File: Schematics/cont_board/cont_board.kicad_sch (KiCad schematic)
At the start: 30 parts, among them IC1 LM2931AZ-5.0_TO92, J1 Conn_01x04, J2 Conn_01x04, J3 Conn_01x04, J4 Conn_01x04, SW1 SW_SPDT, U1 LM317_TO-220, U2 MCP23017_SP

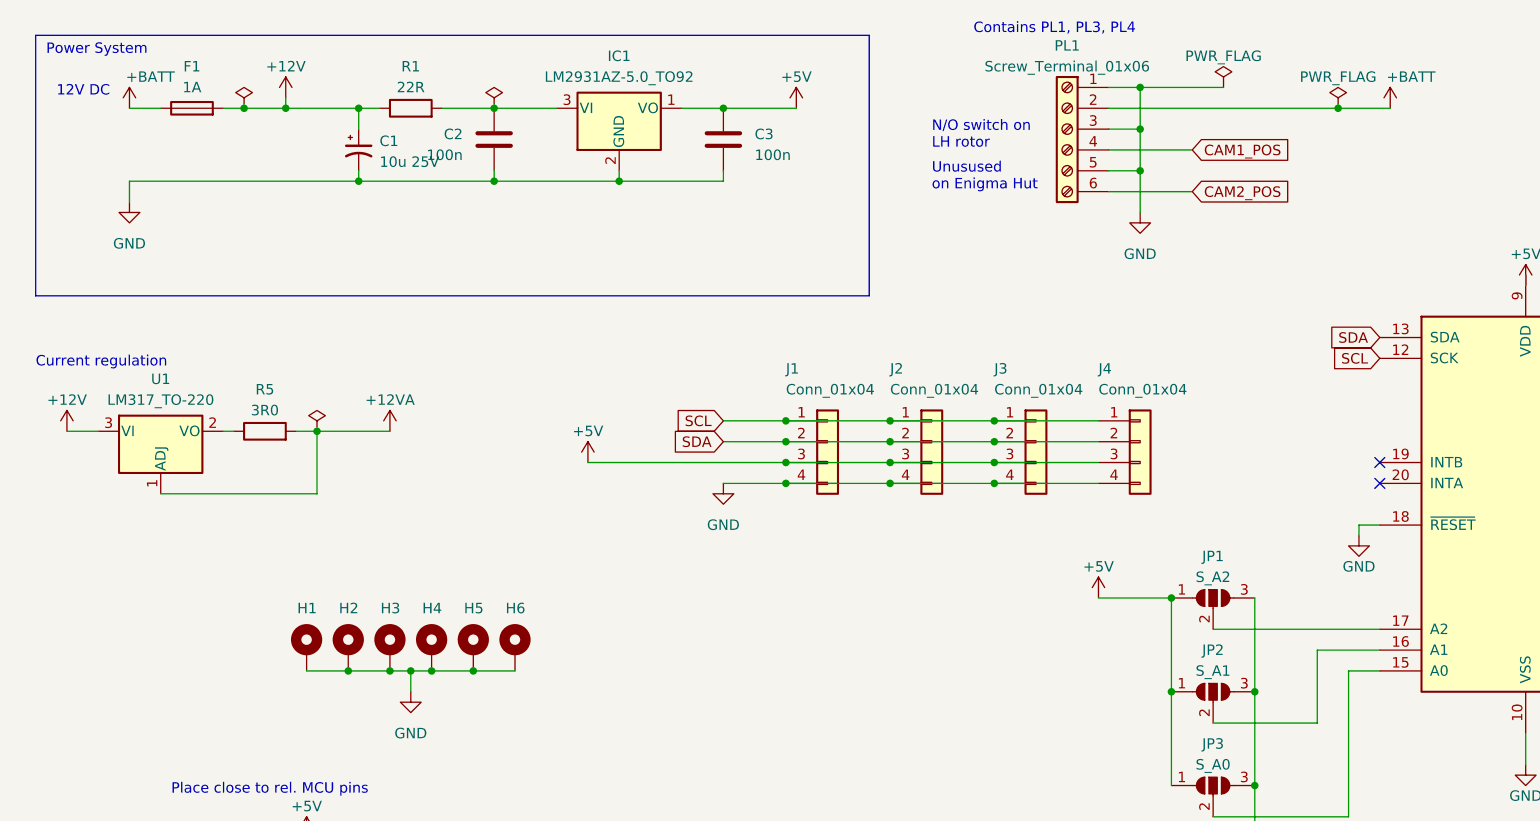
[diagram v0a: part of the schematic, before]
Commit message: Cont-board rev1.1 done and sent to manufacturing
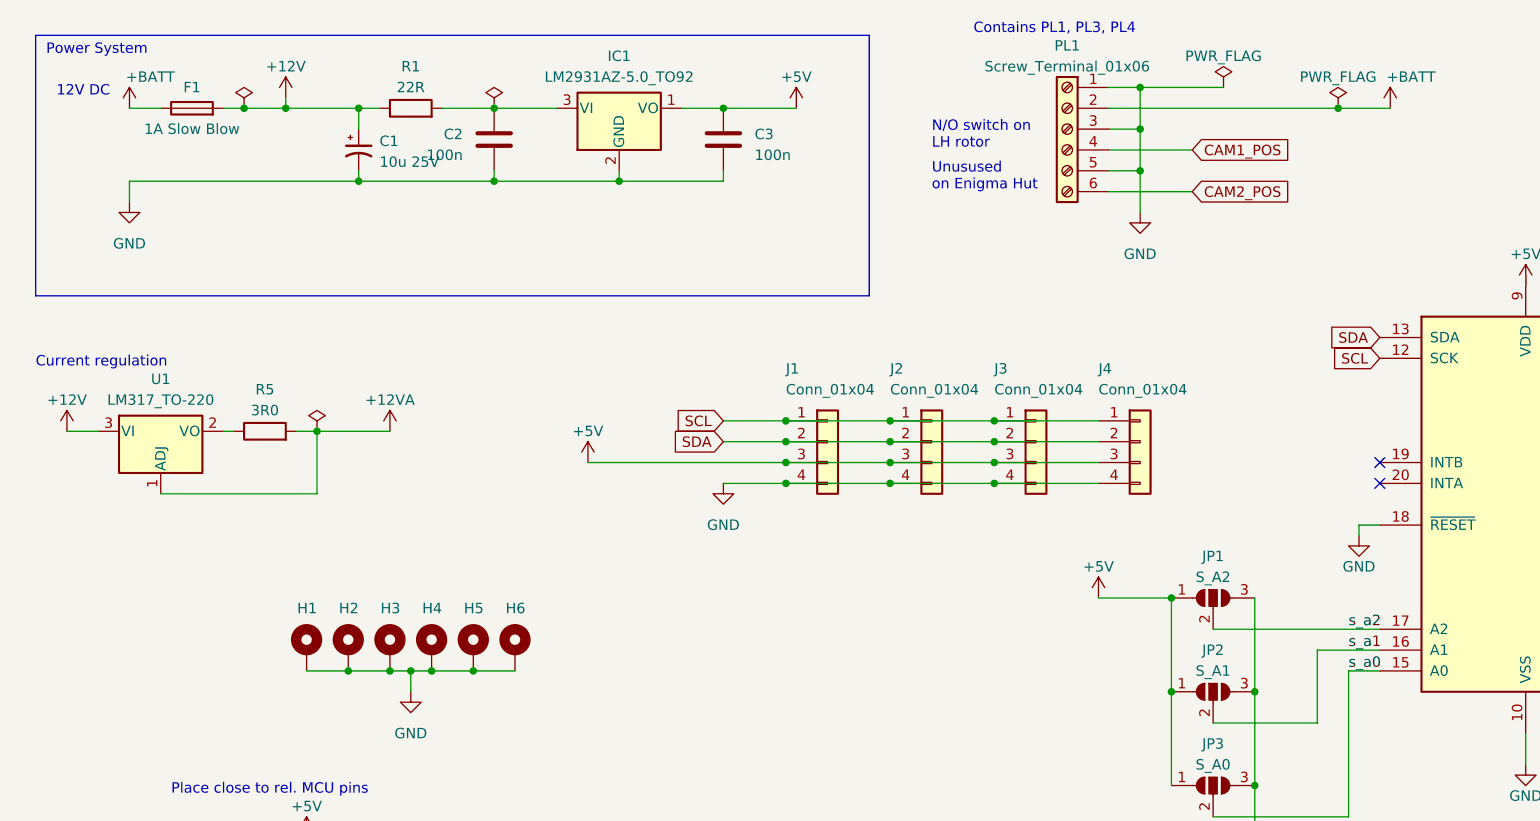
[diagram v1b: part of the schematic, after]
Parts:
- F1: value 1A -> 1A Slow Blow
- J1, J2, J3, J4: footprint Connector_PinHeader_2.54mm:PinHeader_1x04_P2.54mm_Vertical -> user_global_footprints:PinHeader_1x04_P2.54mm_Vertical_SLIM
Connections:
- net s_a0: now reaches JP3.2 (C), U2.15 (A0)
- net s_a1: now reaches JP2.2 (C), U2.16 (A1)
- net s_a2: now reaches JP1.2 (C), U2.17 (A2)
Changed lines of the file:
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@@
+    (effects (font (size 1.27 1.27)) (justify left bottom))
+  )
+  (label "s_a1" (at 175.26 90.17 0) (fields_autoplaced)
+    (effects (font (size 1.27 1.27)) (justify left bottom))
+  )
+  (label "s_a0" (at 175.26 92.71 0) (fields_autoplaced)
+    (effects (font (size 1.27 1.27)) (justify left bottom))
+  )
+  (label "s_a2" (at 175.26 87.63 0) (fields_autoplaced)
     (effects (font (size 1.27 1.27)) (justify left bottom))
   )
@@
       (effects (font (size 1.27 1.27)) (justify left))
     )
-    (property "Footprint" "Connector_PinHeader_2.54mm:PinHeader_1x04_P2.54mm_Vertical" (at 137.16 64.77 0)
+    (property "Footprint" "user_global_footprints:PinHeader_1x04_P2.54mm_Vertical_SLIM" (at 137.16 64.77 0)
       (effects (font (size 1.27 1.27)) hide)
     )
@@
       (effects (font (size 1.27 1.27)) (justify left))
     )
-    (property "Footprint" "Connector_PinHeader_2.54mm:PinHeader_1x04_P2.54mm_Vertical" (at 149.86 64.77 0)
+    (property "Footprint" "user_global_footprints:PinHeader_1x04_P2.54mm_Vertical_SLIM" (at 149.86 64.77 0)
       (effects (font (size 1.27 1.27)) hide)
     )
@@
       (effects (font (size 1.27 1.27)) (justify left))
     )
-    (property "Footprint" "Connector_PinHeader_2.54mm:PinHeader_1x04_P2.54mm_Vertical" (at 124.46 64.77 0)
+    (property "Footprint" "user_global_footprints:PinHeader_1x04_P2.54mm_Vertical_SLIM" (at 124.46 64.77 0)
       (effects (font (size 1.27 1.27)) hide)
     )
@@
   )
   (symbol (lib_id "Device:Fuse") (at 34.29 24.13 90) (unit 1)
-    (in_bom yes) (on_board yes) (dnp no) (fields_autoplaced)
-    (property "Reference" "F1" (at 34.29 19.05 90)
-      (effects (font (size 1.27 1.27)))
-    )
-    (property "Value" "1A" (at 34.29 21.59 90)
+    (in_bom yes) (on_board yes) (dnp no)
+    (property "Reference" "F1" (at 34.29 21.59 90)
+      (effects (font (size 1.27 1.27)))
+    )
+    (property "Value" "1A Slow Blow" (at 34.29 26.67 90)
       (effects (font (size 1.27 1.27)))
     )
@@
       (effects (font (size 1.27 1.27)) (justify left))
     )
-    (property "Footprint" "Connector_PinHeader_2.54mm:PinHeader_1x04_P2.54mm_Vertical" (at 111.76 64.77 0)
-      (effects (font (size 1.27 1.27)) hide)
-    )
+    (property "Footprint" "user_global_footprints:PinHeader_1x04_P2.54mm_Vertical_SLIM" (at 111.76 64.77 0)
+      (effects (font (size 1.27 1.27)) hide)
+    )

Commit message: Lamp Board Work and drl2dxf
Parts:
- R5: value 3R0 -> 2R7
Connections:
- net smth: now reaches C2.1, IC1.3 (VI), R1.2
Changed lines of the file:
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@@
+    (stroke (width 0) (type default))
+  )
+  (wire (pts (xy 71.12 20.32) (xy 71.12 24.13))
     (stroke (width 0) (type default))
   )
@@
   )
   (text "12V DC" (at 17.78 22.86 0)
+    (effects (font (size 1.27 1.27)) (justify left bottom))
+  )
+  (label "smth" (at 71.12 24.13 0) (fields_autoplaced)
     (effects (font (size 1.27 1.27)) (justify left bottom))
   )
@@
       (effects (font (size 1.27 1.27)))
     )
-    (property "Value" "3R0" (at 43.18 60.96 90)
+    (property "Value" "2R7" (at 43.18 60.96 90)
       (effects (font (size 1.27 1.27)))
     )
@@
       (effects (font (size 1.27 1.27)) hide)
     )
-    (property "Datasheet" "https://docs.rs-online.com/e2bc/A700000008799638.G24071932708JIC000" (at 43.18 63.5 0)
+    (property "Datasheet" "https://docs.rs-online.com/e2bc/A700000008799638.pdf" (at 43.18 63.5 0)
       (effects (font (size 1.27 1.27)) hide)
     )
@@
     )
   )
-  (symbol (lib_id "power:PWR_FLAG") (at 71.12 24.13 0) (unit 1)
+  (symbol (lib_id "power:PWR_FLAG") (at 71.12 20.32 0) (unit 1)
     (in_bom yes) (on_board yes) (dnp no) (fields_autoplaced)
-    (property "Reference" "#FLG03" (at 71.12 22.225 0)
-      (effects (font (size 1.27 1.27)) hide)
-    )
-    (property "Value" "PWR_FLAG" (at 71.12 20.32 0)
-      (effects (font (size 1.27 1.27)) hide)
-    )
-    (property "Footprint" "" (at 71.12 24.13 0)
-      (effects (font (size 1.27 1.27)) hide)
-    )
-    (property "Datasheet" "~" (at 71.12 24.13 0)
-      (effects (font (size 1.27 1.27)) hide)
-    )
+    (property "Reference" "#FLG03" (at 71.12 18.415 0)
+      (effects (font (size 1.27 1.27)) hide)
+    )
+    (property "Value" "PWR_FLAG" (at 71.12 16.51 0)
+      (effects (font (size 1.27 1.27)) hide)
+    )
+    (property "Footprint" "" (at 71.12 20.32 0)
+      (effects (font (size 1.27 1.27)) hide)
+    )
+    (property "Datasheet" "~" (at 71.12 20.32 0)
+      (effects (font (size 1.27 1.27)) hide)
+    )

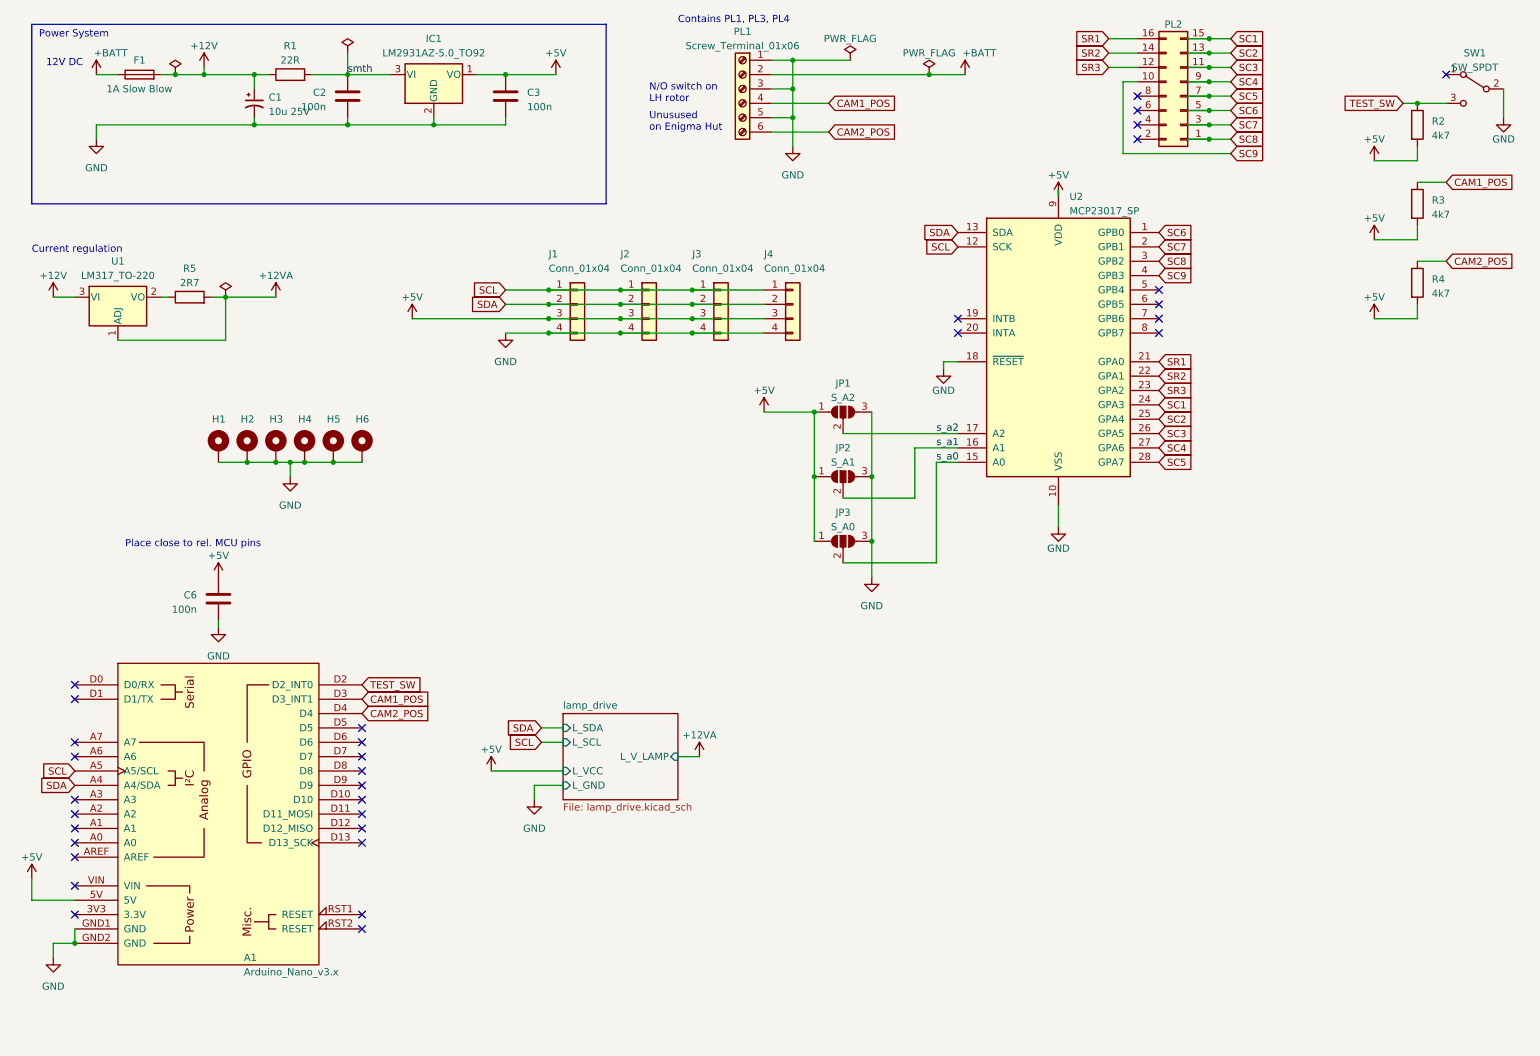
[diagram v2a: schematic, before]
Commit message: Fixed error - mcp rst tied to gnd
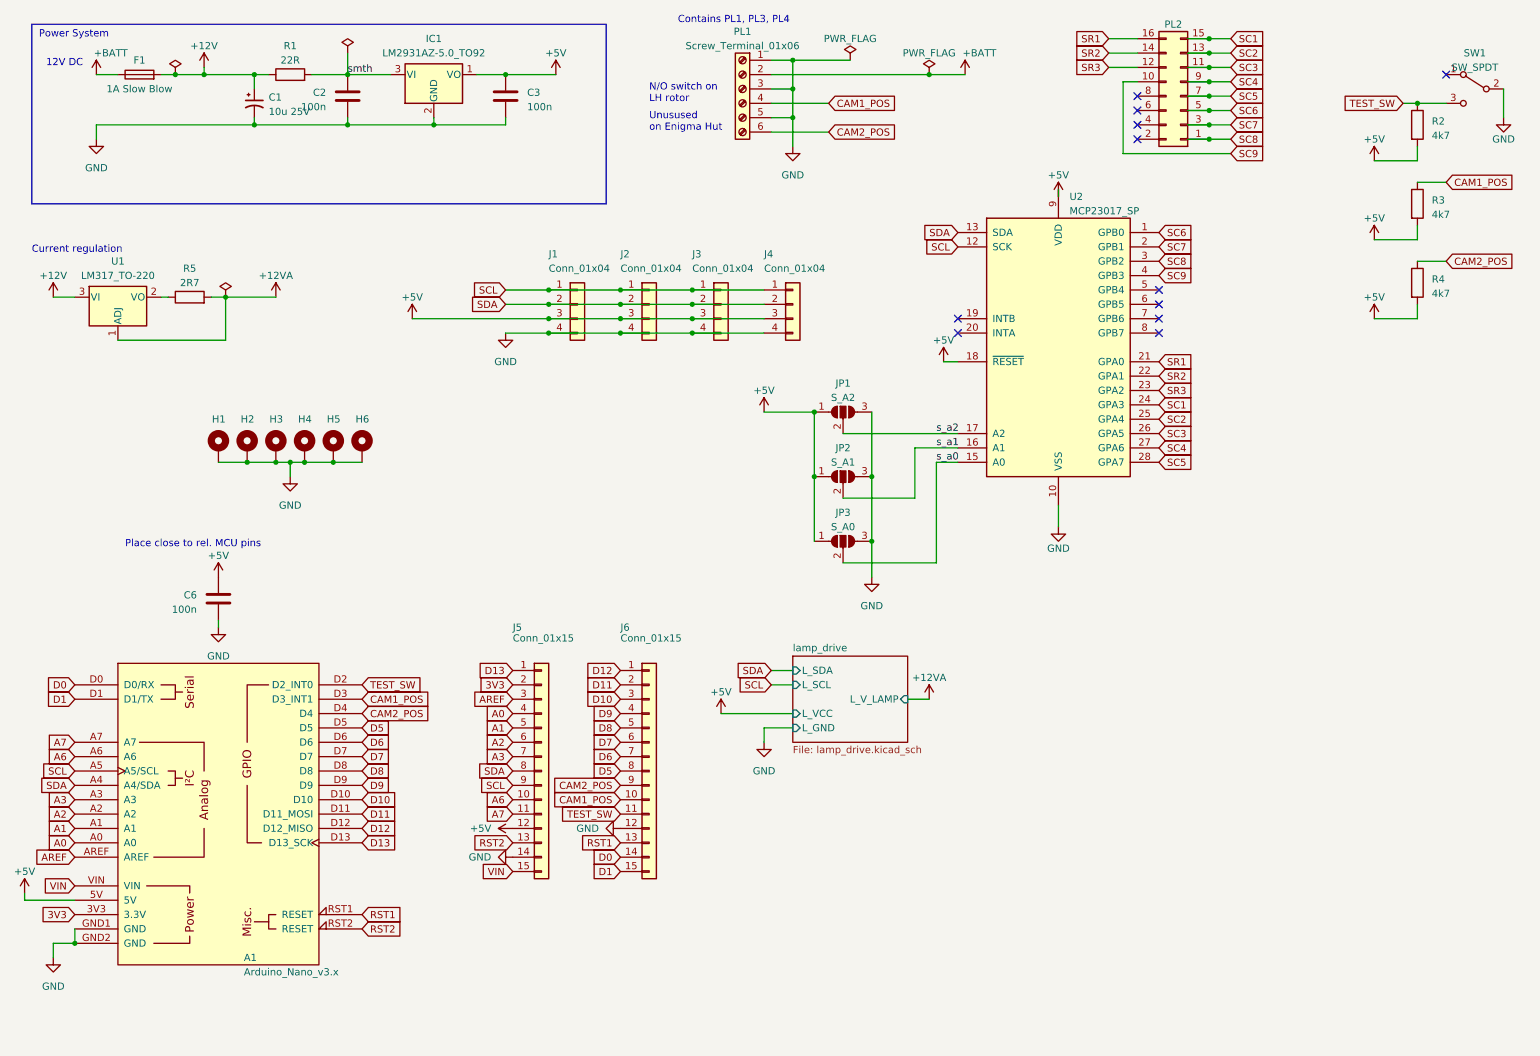
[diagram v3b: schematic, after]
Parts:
- added J5, J6: Conn_01x15, Connector_PinHeader_2.54mm:PinHeader_1x15_P2.54mm_Vertical, symbol Connector_Generic:Conn_01x15
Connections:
- net +5V: now also U2.18 (~{RESET}), J5.12 (Pin_12)
- net CAM1_POS: now also J6.10 (Pin_10)
- net CAM2_POS: now also J6.9 (Pin_9)
- net GND: now also J5.14 (Pin_14), J6.12 (Pin_12); no longer U2.18 (~{RESET})
- net SCL: now also J5.9 (Pin_9)
- net SDA: now also J5.8 (Pin_8)
- net TEST_SW: now also J6.11 (Pin_11)
- net 3V3: now reaches A1.3V3 (3.3V)
- net 3V3: now also J5.2 (Pin_2)
- net A0: now reaches A1.A0
- net A0: now also J5.4 (Pin_4)
- net A1: now reaches A1.A1
- net A1: now also J5.5 (Pin_5)
- net A2: now reaches A1.A2
- net A2: now also J5.6 (Pin_6)
- net A3: now reaches A1.A3
- net A3: now also J5.7 (Pin_7)
- net A6: now reaches A1.A6
- net A6: now also J5.10 (Pin_10)
- net A7: now reaches A1.A7
- net A7: now also J5.11 (Pin_11)
- net AREF: now reaches A1.AREF
- net AREF: now also J5.3 (Pin_3)
- net D0: now reaches A1.D0 (D0/RX)
- net D0: now also J6.14 (Pin_14)
- net D1: now reaches A1.D1 (D1/TX)
- net D1: now also J6.15 (Pin_15)
- net D10: now reaches A1.D10
- net D10: now also J6.3 (Pin_3)
- net D11: now reaches A1.D11 (D11_MOSI)
- net D11: now also J6.2 (Pin_2)
- net D12: now reaches A1.D12 (D12_MISO)
- net D12: now also J6.1 (Pin_1)
- net D13: now reaches A1.D13 (D13_SCK)
- net D13: now also J5.1 (Pin_1)
- net D5: now reaches A1.D5
- net D5: now also J6.8 (Pin_8)
- net D6: now reaches A1.D6
- net D6: now also J6.7 (Pin_7)
- net D7: now reaches A1.D7
- net D7: now also J6.6 (Pin_6)
- net D8: now reaches A1.D8
- net D8: now also J6.5 (Pin_5)
- net D9: now reaches A1.D9
- net D9: now also J6.4 (Pin_4)
- net RST1: now reaches A1.RST1 (RESET)
- net RST1: now also J6.13 (Pin_13)
- net RST2: now reaches A1.RST2 (RESET)
- net RST2: now also J5.13 (Pin_13)
- net VIN: now reaches A1.VIN
- net VIN: now also J5.15 (Pin_15)
- no-connect marks 33 -> 11

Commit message: Final Commit
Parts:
- added J13: Conn_02x03_Counter_Clockwise, user_global_footprints:PinHeader_2x03_P2.54mm_Horizontal_Short_Pins, symbol Connector_Generic:Conn_02x03_Counter_Clockwise
- added R6, R7: 4k7, Resistor_THT:R_Axial_DIN0207_L6.3mm_D2.5mm_P10.16mm_Horizontal, symbol Device:R
- H1, H2, H3, H4, H5, H6: footprint MountingHole:MountingHole_3.2mm_M3_Pad_Via -> user_global_footprints:MountingHole_4mm_Pad_Via
- J4: value Conn_01x04 -> PBOARD_CONN; footprint user_global_footprints:PinHeader_1x04_P2.54mm_Vertical_SLIM -> Connector_PinHeader_2.54mm:PinHeader_1x04_P2.54mm_Horizontal
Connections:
- net +5V: now also J13.6 (Pin_6), R6.1, R7.1
- net D11: now also J13.5 (Pin_5)
- net D12: now also J13.1 (Pin_1)
- net D13: now also J13.2 (Pin_2)
- net GND: now also J13.4 (Pin_4)
- net RST2: now also J13.3 (Pin_3)
- net SCL: now also R6.2
- net SDA: now also R7.2
- net VIN: no longer names the net of J5.15 (Pin_15)
- net VIN: no longer A1.VIN
- no-connect marks 11 -> 13
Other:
- added sheet RotorEncoder (rotor_drive.kicad_sch)
- added sheet RotorEncoder1 (rotor_drive.kicad_sch)
- added sheet RotorEncoder2 (rotor_drive.kicad_sch)
- note added: "ICSP"
- company: (none) -> CUED
- title: EngimaHut Switch Board -> LZB23 - Enigma Control Board
- moved on the sheet: A1, C6, H1, H2, H3, H4, H5, H6, J1, J2, J3, J4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
